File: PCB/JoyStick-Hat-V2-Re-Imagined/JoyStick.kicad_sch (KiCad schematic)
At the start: 18 parts, among them J14 Conn_01x03_Pin, J15 Conn_01x03_Pin, J4 Conn_02x04_Odd_Even, J8 Conn_02x04_Odd_Even

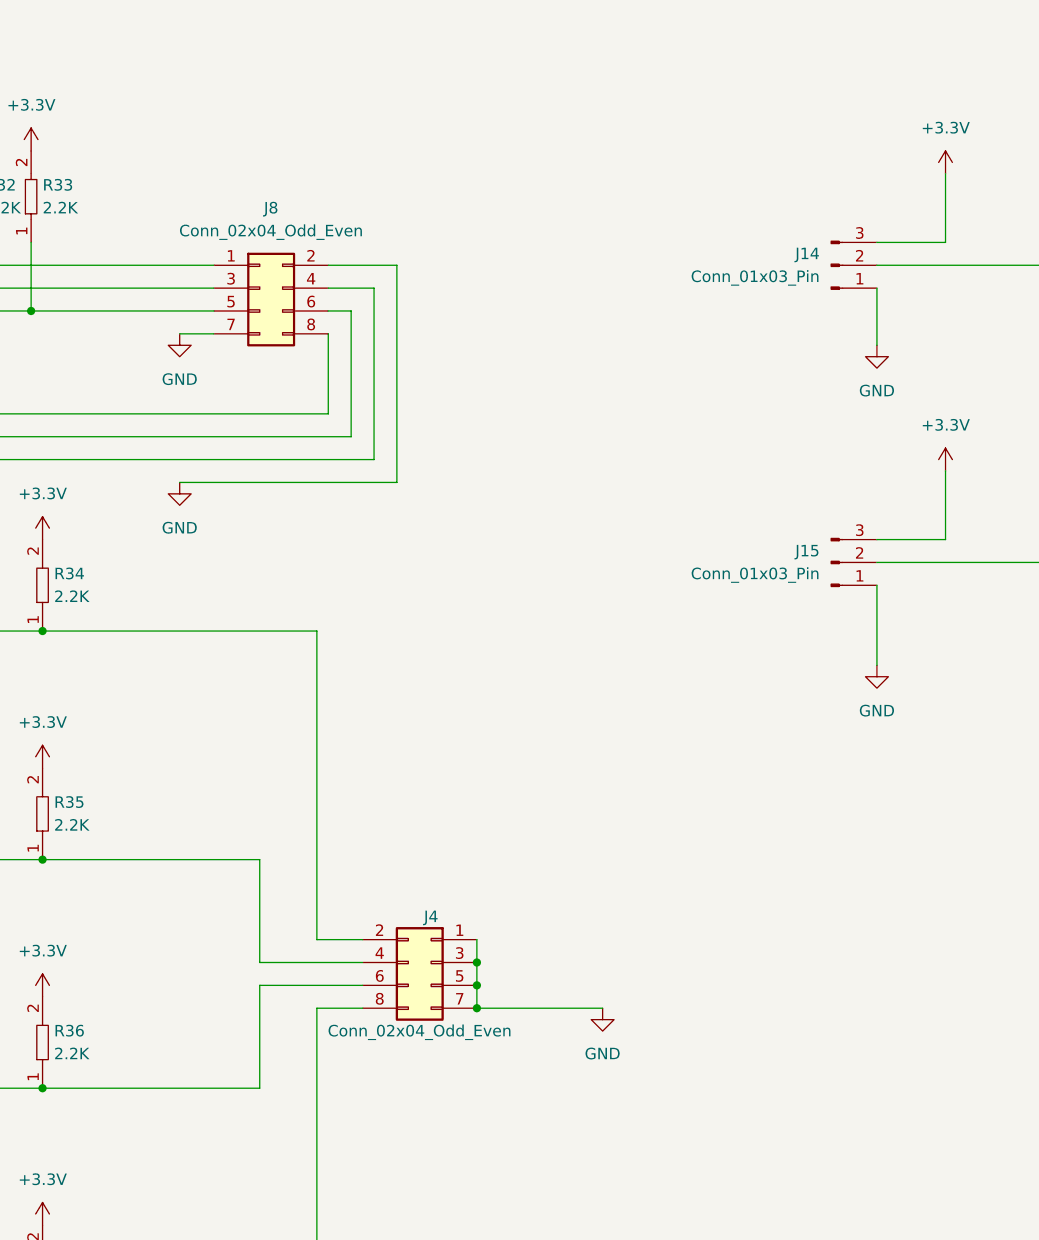
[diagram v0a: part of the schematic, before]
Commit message: V2
Lots of progress made on version two of JoyStick Hat but the RPi 5 is going to be elimintated and an additional RS485 port added.
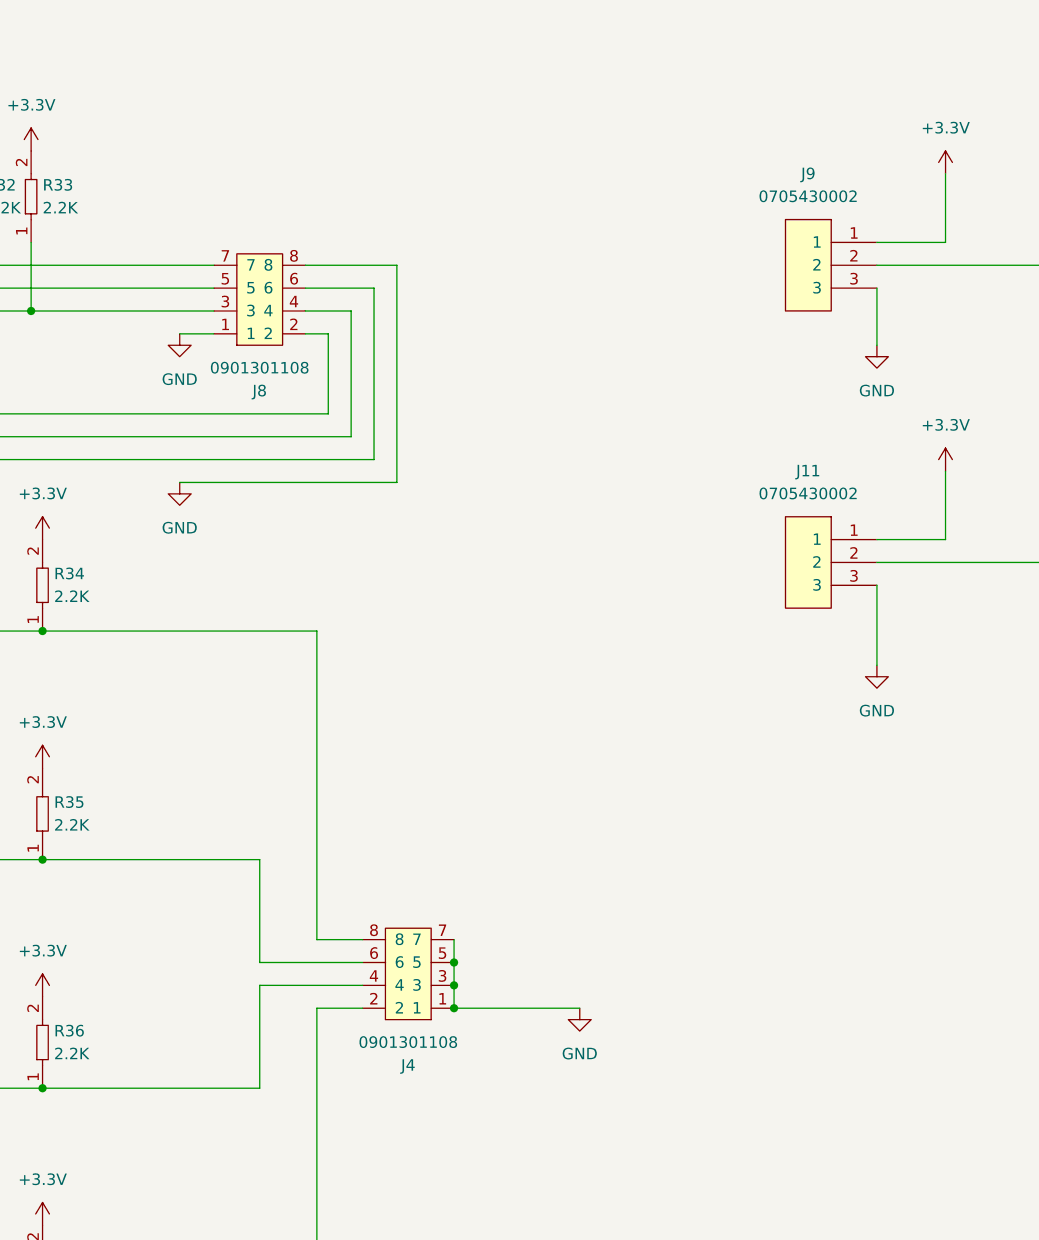
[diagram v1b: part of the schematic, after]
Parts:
- removed J14, J15: Conn_01x03_Pin, Connector_PinHeader_2.54mm:PinHeader_1x03_P2.54mm_Vertical, symbol Connector:Conn_01x03_Pin
- removed J4, J8: Conn_02x04_Odd_Even, Connector_PinHeader_2.54mm:PinHeader_2x04_P2.54mm_Vertical, symbol Connector_Generic:Conn_02x04_Odd_Even
- added J11, J9: 0705430002, AVR-KiCAD-Lib-Connectors:Shrouded_Pin_Header_Straight_1x03_Pitch2.54mm, symbol AVR-KiCAD-Lib-Connectors:0705430002
- added J4, J8: 0901301108, AVR-KiCAD-Lib-Connectors:CON_901301108_MOL, symbol AVR-KiCAD-Lib-Connectors:0901301108
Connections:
- net +3.3V: now also J11.1, J9.1
- net BUTTON1: now also J4.8
- net BUTTON2: now also J4.6
- net BUTTON3: now also J4.4
- net BUTTON4: now also J4.2
- net GND: now also J11.3, J4.1, J4.3, J4.5, J4.7, J8.1, J8.8, J9.3
- net JOYSTICK_X: now also J9.2
- net JOYSTICK_Y: now also J11.2
- net ROTARY1_POLE1: now also J8.7
- net ROTARY1_POLE2: now also J8.5
- net ROTARY1_POLE3: now also J8.3
- net ROTARY2_POLE1: now also J8.2
- net ROTARY2_POLE2: now also J8.4
- net ROTARY2_POLE3: now also J8.6
